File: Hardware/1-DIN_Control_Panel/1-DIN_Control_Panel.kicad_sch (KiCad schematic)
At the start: 30 parts, among them J1 Conn_01x09, J3 Pot/SW - Brightness, K1 Relay_SPDT, U2 LM324A

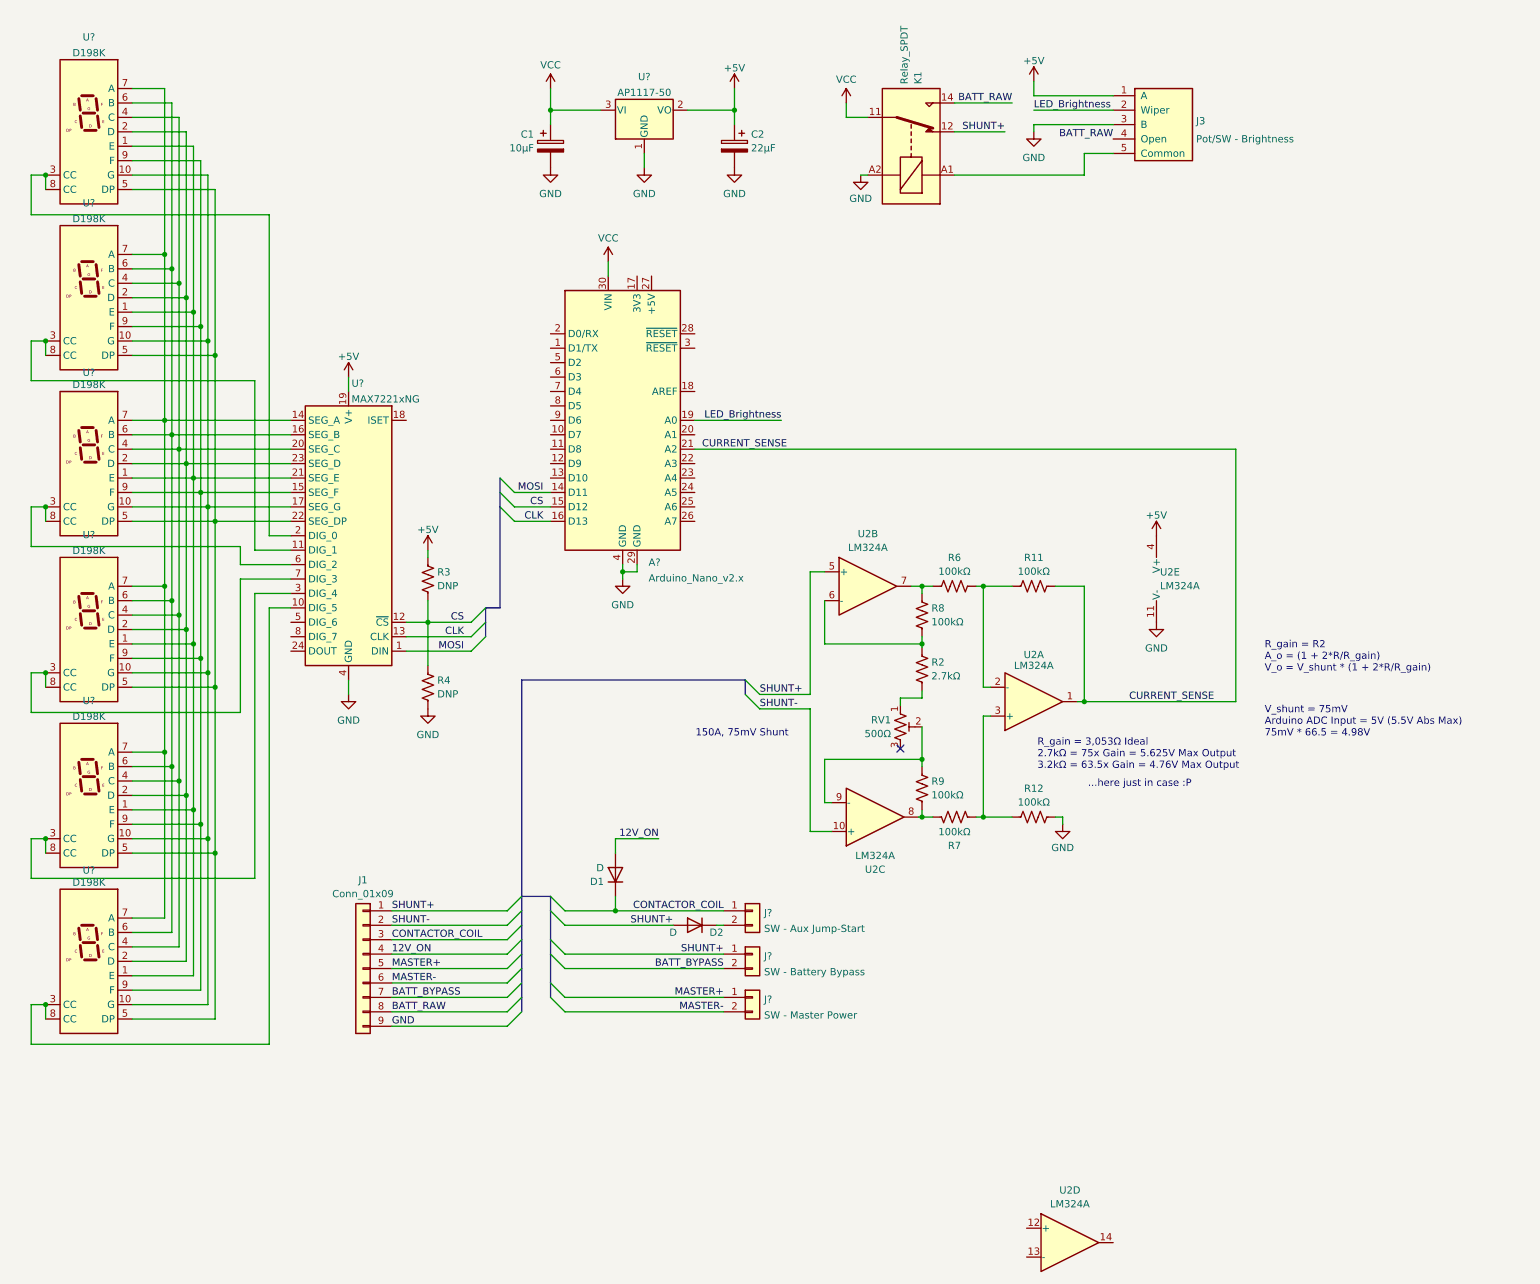
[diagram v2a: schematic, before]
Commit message: Assigned footprints, expanded schematic
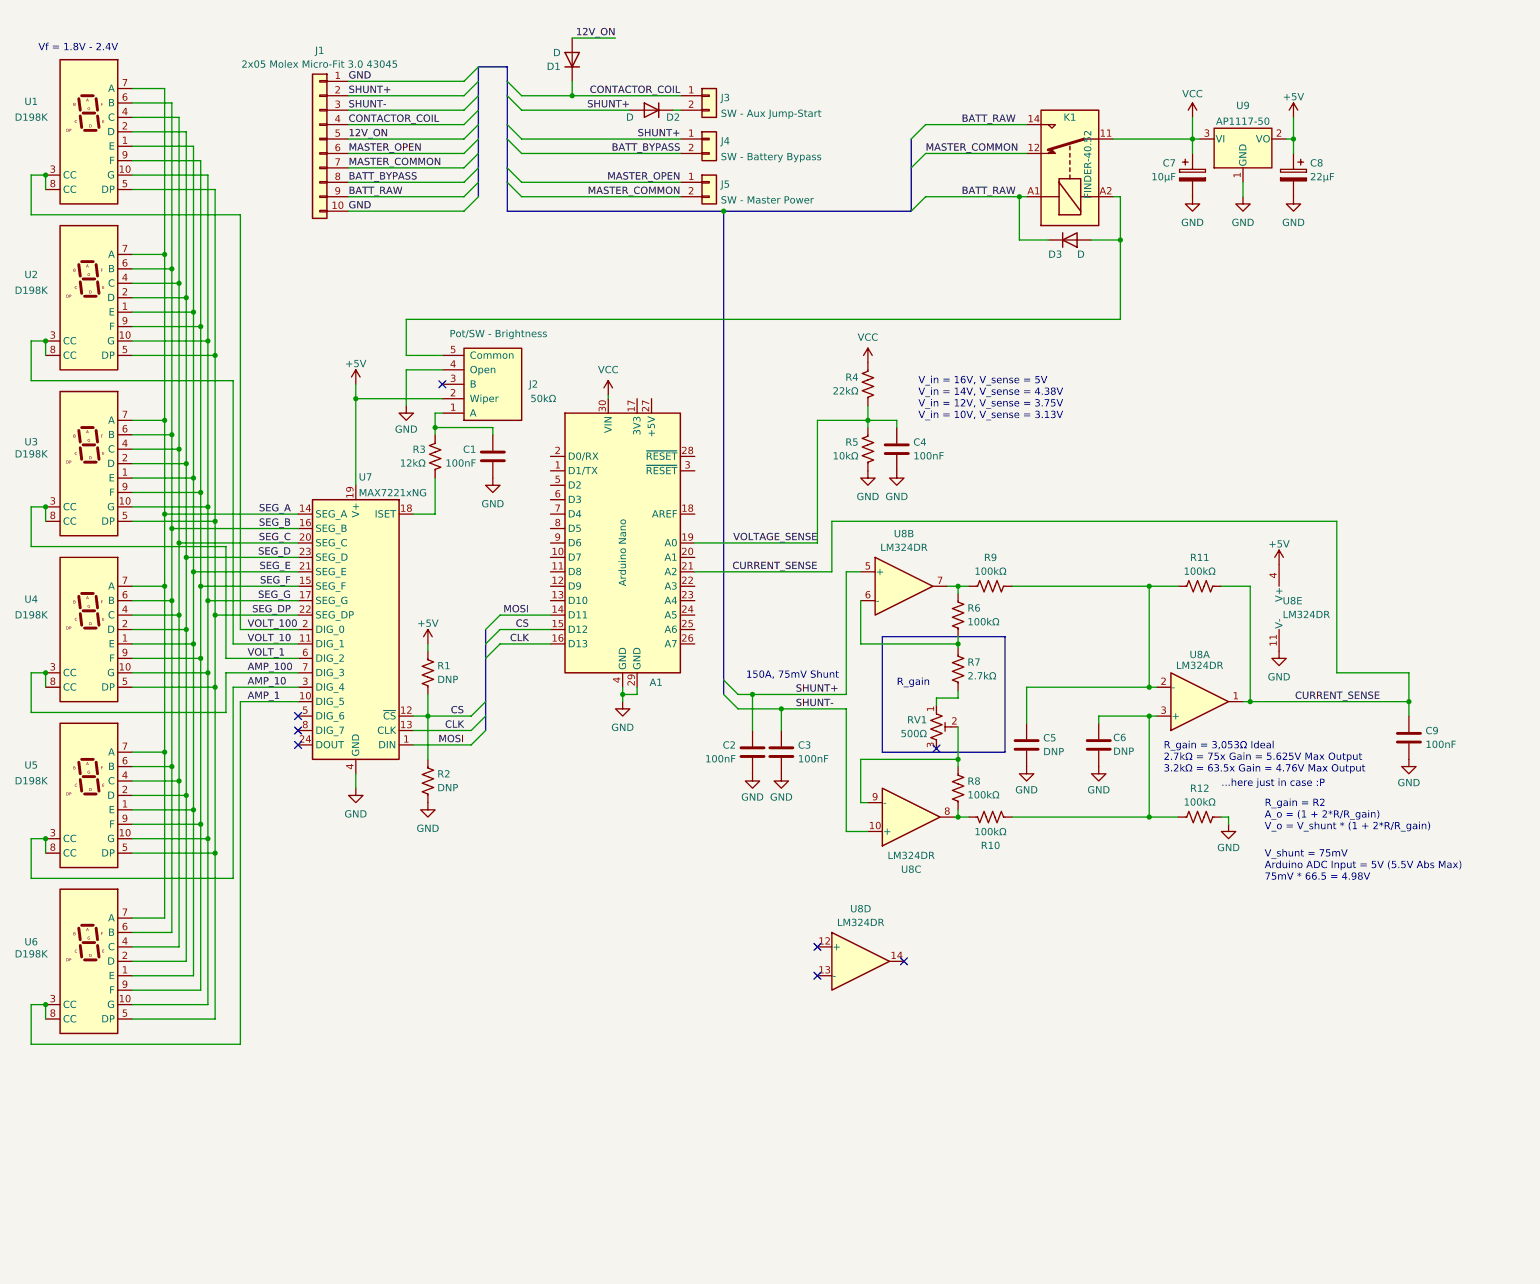
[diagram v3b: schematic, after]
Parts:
- removed J?: SW - Master Power, symbol Connector_Generic:Conn_01x02
- removed J?: SW - Battery Bypass, symbol Connector_Generic:Conn_01x02
- removed K1: Relay_SPDT, symbol Relay:Relay_SPDT
- added C1, C2, C3, C4, C9: 100nF, Capacitor_SMD:C_0603_1608Metric_Pad1.08x0.95mm_HandSolder, symbol Device:C
- added C5, C6: DNP, Capacitor_SMD:C_0603_1608Metric_Pad1.08x0.95mm_HandSolder, symbol Device:C
- added D3: D, Diode_THT:D_A-405_P2.54mm_Vertical_AnodeUp, symbol Device:D
- added J4: SW - Battery Bypass, Connector_Molex:Molex_Micro-Fit_3.0_43045-0212_2x01_P3.00mm_Vertical, symbol Connector_Generic:Conn_01x02
- added J5: SW - Master Power, Connector_Molex:Molex_Micro-Fit_3.0_43045-0212_2x01_P3.00mm_Vertical, symbol Connector_Generic:Conn_01x02
- added K1: FINDER-40.52, Relay_THT:Relay_DPDT_Finder_30.22, symbol Relay:FINDER-40.51
- added R3: 12kΩ, Resistor_SMD:R_0603_1608Metric_Pad0.98x0.95mm_HandSolder, symbol Device:R_US
- added R4: 22kΩ, Resistor_SMD:R_0603_1608Metric_Pad0.98x0.95mm_HandSolder, symbol Device:R_US
- added R5: 10kΩ, Resistor_SMD:R_0603_1608Metric_Pad0.98x0.95mm_HandSolder, symbol Device:R_US
- A1: renamed from A?; value Arduino_Nano_v2.x -> Arduino Nano
- C7: renamed from C1; footprint (none) -> Capacitor_SMD:C_0603_1608Metric_Pad1.08x0.95mm_HandSolder
- C8: renamed from C2; footprint (none) -> Capacitor_SMD:C_0603_1608Metric_Pad1.08x0.95mm_HandSolder
- D1, D2: footprint (none) -> Diode_THT:D_A-405_P2.54mm_Vertical_AnodeUp
- J1: value Conn_01x09 -> 2x05 Molex Micro-Fit 3.0 43045; footprint (none) -> Connector_Molex:Molex_Micro-Fit_3.0_43045-1012_2x05_P3.00mm_Vertical; symbol Connector_Generic:Conn_01x09 -> Connector_Generic:Conn_01x10; DigiKey (none) -> https://www.digikey.com/en/products/detail/molex/0430451027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
- J2: renamed from J3; footprint (none) -> TerminalBlock:TerminalBlock_bornier-5_P5.08mm; Field4 (none) -> 50kΩ
- J3: renamed from J?; footprint (none) -> Connector_Molex:Molex_Micro-Fit_3.0_43045-0212_2x01_P3.00mm_Vertical; Digikey (none) -> https://www.digikey.com/en/products/detail/molex/0430450212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
- R1: renamed from R3; footprint (none) -> Resistor_SMD:R_0603_1608Metric_Pad0.98x0.95mm_HandSolder
- R10: renamed from R7; footprint (none) -> Resistor_SMD:R_0603_1608Metric_Pad0.98x0.95mm_HandSolder
- R11, R12: footprint (none) -> Resistor_SMD:R_0603_1608Metric_Pad0.98x0.95mm_HandSolder
- R2: renamed from R4; footprint (none) -> Resistor_SMD:R_0603_1608Metric_Pad0.98x0.95mm_HandSolder
- R6: renamed from R8; footprint (none) -> Resistor_SMD:R_0603_1608Metric_Pad0.98x0.95mm_HandSolder
- R7: renamed from R2; footprint (none) -> Resistor_SMD:R_0603_1608Metric_Pad0.98x0.95mm_HandSolder
- R8: renamed from R9; footprint (none) -> Resistor_SMD:R_0603_1608Metric_Pad0.98x0.95mm_HandSolder
- R9: renamed from R6; footprint (none) -> Resistor_SMD:R_0603_1608Metric_Pad0.98x0.95mm_HandSolder
- RV1: footprint (none) -> Buzzer_Beeper:Buzzer_12x9.5RM7.6
- U8: renamed from U2; value LM324A -> LM324DR; footprint (none) -> Package_SO:SOIC-14_3.9x8.7mm_P1.27mm
- gave numbers to parts that had none: 8
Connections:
- net MASTER+ is gone; now on net 12V_ON: J1.5 (Pin_5)
- net +5V: now also J2.2 (Wiper); no longer J2.1 (A)
- net 12V_ON: no longer J1.4 (Pin_4)
- net BATT_BYPASS: now also J1.8 (Pin_8), J4.2 (Pin_2); no longer J1.7 (Pin_7)
- net BATT_RAW: now also J1.9 (Pin_9), D3.1 (K), K1.14, K1.A1; no longer J1.8 (Pin_8), J2.4 (Open)
- net CONTACTOR_COIL: now also J1.4 (Pin_4); no longer J1.3 (Pin_3)
- net CURRENT_SENSE: now also C9.1
- net GND: now also J1.1 (Pin_1), J1.10 (Pin_10), J2.4 (Open), C1.2, C2.2, C3.2, C4.2, C5.2, C6.2, C9.2, R5.1; no longer J1.9 (Pin_9), J2.3 (B)
- net SHUNT+: now also J1.2 (Pin_2), C2.1, J4.1 (Pin_1); no longer J1.1 (Pin_1)
- net SHUNT-: now also J1.3 (Pin_3), C3.1; no longer J1.2 (Pin_2)
- net VCC: now also K1.11, R4.2
- net at R11.1, R9.2, U8.2 (-): now also C5.1
- net at R10.2, R12.1, U8.3 (+): now also C6.1
- net SEG_E: now reaches U1.1 (E), U2.1 (E), U3.1 (E), U4.1 (E), U5.1 (E), U6.1 (E), U7.21 (SEG_E)
- net SEG_G: now reaches U1.10 (G), U2.10 (G), U3.10 (G), U4.10 (G), U5.10 (G), U6.10 (G), U7.17 (SEG_G)
- net SEG_D: now reaches U1.2 (D), U2.2 (D), U3.2 (D), U4.2 (D), U5.2 (D), U6.2 (D), U7.23 (SEG_D)
- net AMP_10: now reaches U5.3 (CC), U5.8 (CC), U7.3 (DIG_4)
- net SEG_C: now reaches U1.4 (C), U2.4 (C), U3.4 (C), U4.4 (C), U5.4 (C), U6.4 (C), U7.20 (SEG_C)
- net SEG_DP: now reaches U1.5 (DP), U2.5 (DP), U3.5 (DP), U4.5 (DP), U5.5 (DP), U6.5 (DP), U7.22 (SEG_DP)
- net SEG_B: now reaches U1.6 (B), U2.6 (B), U3.6 (B), U4.6 (B), U5.6 (B), U6.6 (B), U7.16 (SEG_B)
- net SEG_A: now reaches U1.7 (A), U2.7 (A), U3.7 (A), U4.7 (A), U5.7 (A), U6.7 (A), U7.14 (SEG_A)
- net SEG_F: now reaches U1.9 (F), U2.9 (F), U3.9 (F), U4.9 (F), U5.9 (F), U6.9 (F), U7.15 (SEG_F)
- net VOLT_1: now reaches U3.3 (CC), U3.8 (CC), U7.6 (DIG_2)
- net VOLT_10: now reaches U2.3 (CC), U2.8 (CC), U7.11 (DIG_1)
- net at J2.5 (Common): now also D3.2 (A), K1.A2
- net VOLT_100: now reaches U1.3 (CC), U1.8 (CC), U7.2 (DIG_0)
- net AMP_1: now reaches U6.3 (CC), U6.8 (CC), U7.10 (DIG_5)
- net AMP_100: now reaches U4.3 (CC), U4.8 (CC), U7.7 (DIG_3)
- net at U7.18 (ISET): now also R3.1
- net LED_Brightness renamed VOLTAGE_SENSE
- net VOLTAGE_SENSE: now also C4.1, R4.1, R5.2; no longer J2.2 (Wiper)
- net MASTER- renamed MASTER_OPEN
- net MASTER_OPEN: now also J5.1 (Pin_1)
- new net: C1.1, J2.1 (A), R3.2
- new net MASTER_COMMON: J1.7 (Pin_7), J5.2 (Pin_2), K1.12
- no-connect marks 1 -> 8
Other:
- note added: "R_gain"
- note added: "V_in = 16V, V_sense = 5V V_in = 14V, V_sense = 4.38V V_in = 12V, V_sense = 3.75V V_in = 10V, V_sense = 3.13V"
- note added: "Vf = 1.8V - 2.4V"
- moved on the sheet: A1, C7, C8, D1, D2, J2, J3, R1, R10, R11, R12, R2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

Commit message: Changed to 14-segement Characters
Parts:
- removed C1: 100nF, Capacitor_SMD:C_0603_1608Metric_Pad1.08x0.95mm_HandSolder, symbol Device:C
- removed C8: 22µF, Capacitor_SMD:C_0603_1608Metric_Pad1.08x0.95mm_HandSolder, symbol Device:C_Polarized
- removed R2: DNP, Resistor_SMD:R_0603_1608Metric_Pad0.98x0.95mm_HandSolder, symbol Device:R_US
- removed R3: 12kΩ, Resistor_SMD:R_0603_1608Metric_Pad0.98x0.95mm_HandSolder, symbol Device:R_US
- removed U1, U2, U3, U4, U5, U6: D198K, Display_7Segment:D1X8K, symbol Display_Character:D198K
- removed U7: MAX7221xNG, Package_DIP:DIP-24_W7.62mm, symbol Driver_LED:MAX7221xNG
- removed U9: AP1117-50, Package_TO_SOT_SMD:SOT-223-3_TabPin2, symbol Regulator_Linear:AP1117-50
- added C1: 10µF, Capacitor_SMD:C_0603_1608Metric_Pad1.08x0.95mm_HandSolder, symbol Device:C_Polarized
- added C10: 22µF, Capacitor_SMD:C_0603_1608Metric_Pad1.08x0.95mm_HandSolder, symbol Device:C_Polarized
- added C8: 100nF, Capacitor_SMD:C_0603_1608Metric_Pad1.08x0.95mm_HandSolder, symbol Device:C
- added D10, D4, D5, D6, D7, D8, D9: LED_Filled, symbol Device:LED_Filled
- added F1: 1A Trip, Fuse:Fuse_Bourns_MF-RG300, symbol Device:Polyfuse_Small
- added J6: Mode Controller, Connector_Molex:Molex_Micro-Fit_3.0_43045-0812_2x04_P3.00mm_Vertical, symbol Connector:8P8C_Shielded
- added J?: Rotary Switch 1x7, Connector_Molex:Molex_Micro-Fit_3.0_43045-0812_2x04_P3.00mm_Vertical, symbol Connector_Generic:Conn_01x08
- added R13, R14, R15, R16, R17, R18, R19: 680Ω, Resistor_SMD:R_0603_1608Metric_Pad0.98x0.95mm_HandSolder, symbol Device:R_US
- added U1, U2: LTV-847S, Package_DIP:SMDIP-16_W9.53mm, symbol Isolator:LTV-847S
- added U10: CA56-12SEKWA, Display_7Segment:CA56-12SEKWA, symbol Panel_Parts:COM-21212
- added U3: MAX 6954 - SSOP, symbol Panel_Parts:MAX_6954-SSOP
- added U4: 12V->5V Variable Boost Buck Converter, libraries:BoostBuck, symbol library_symbols:12V Variable Boost Buck Converter
- C7: value 10µF -> 47µF
- R1: value DNP -> 10kΩ
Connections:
- net +5V: now also A1.27 (+5V), C10.1, U1.10, U4.3 (+VOUT); no longer R1.1
- net GND: now also R1.1, C1.2, C10.2, J6.SH, U1.11, U1.13, U1.15, U2.11, U2.13, U2.15, U2.9, U4.2 (-VIN), U4.4 (-VOUT); no longer C7.2
- net VCC: now also C1.1, F1.2, U4.1 (+VIN); no longer A1.30 (VIN), C7.1, K1.11
- net Arduino_~{CS}: now reaches A1.13 (D10)
- net Arduino_~{CS}: now also U3.3 (~{CS})
- net CLK renamed Arduino_SCK
- net Arduino_SCK: now also U3.5 (CLK)
- net CS renamed Arduino_MISO
- net Arduino_MISO: now also U3.4 (DOUT); no longer R1.2
- net MOSI renamed Arduino_MOSI
- net Arduino_MOSI: now also U3.6 (DIN)
- new net: D9.1 (K), U1.14
- new net: D9.2 (A), R18.2
- new net: D10.1 (K), U1.12
- new net: D10.2 (A), R19.2
- new net: F1.1, K1.11
- new net: D4.1 (K), U2.16
- new net: D4.2 (A), R13.2
- new net: D8.2 (A), R17.2
- new net: J?.5 (Pin_5), U1.1
- new net: D8.1 (K), U1.16
- new net: D6.1 (K), U2.12
- new net: J?.3 (Pin_3), U2.5
- new net: D7.2 (A), R16.2
- new net: D6.2 (A), R15.2
- new net: D5.1 (K), U2.14
- new net: J?.2 (Pin_2), U2.3
- new net: D7.1 (K), U2.10
- new net: J?.4 (Pin_4), U2.7
- new net: J?.1 (Pin_1), U2.1
- new net: J?.6 (Pin_6), U1.3
- new net: J?.7 (Pin_7), U1.5
- new net: J?.8 (Pin_8), U1.8
- new net: D5.2 (A), R14.2
- new net MODE_1: J6.8, U2.2
- new net MODE_12V: J6.1, U1.7
- new net MODE_1_LED: R13.1
- new net MODE_2: J6.7, U2.4
- new net MODE_2_LED: R14.1
- new net MODE_3: J6.6, U2.6
- new net MODE_3_LED: R15.1
- new net MODE_4: J6.5, U2.8
- new net MODE_4_LED: R16.1
- new net MODE_5: J6.4, U1.2
- new net MODE_5_LED: R17.1
- new net MODE_6: J6.3, U1.4
- new net MODE_6_LED: R18.1
- new net MODE_7: J6.2, U1.6
- new net MODE_7_LED: R19.1
- new net MODE_PWR_DETECT: R1.2, U1.9
- no-connect marks 8 -> 5
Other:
- note added: "MAKE A FOOTPRINT FOR THIS"
- note added: "Mode Selector LED PWM Brightness Control"
- note added: "Using extra optoisolator as mode selector 12V detect signal...because why not!"
- note removed: "Vf = 1.8V - 2.4V"
- moved on the sheet: A1, C2, C3, C4, C5, C6, C9, D1, D2, D3, J1, J2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
